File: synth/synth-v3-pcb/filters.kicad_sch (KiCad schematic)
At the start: 44 parts, among them J4 3.5mm Jack, U1 LM324N, U2 LM324N, U3 LM324N, U6 NJM4580D

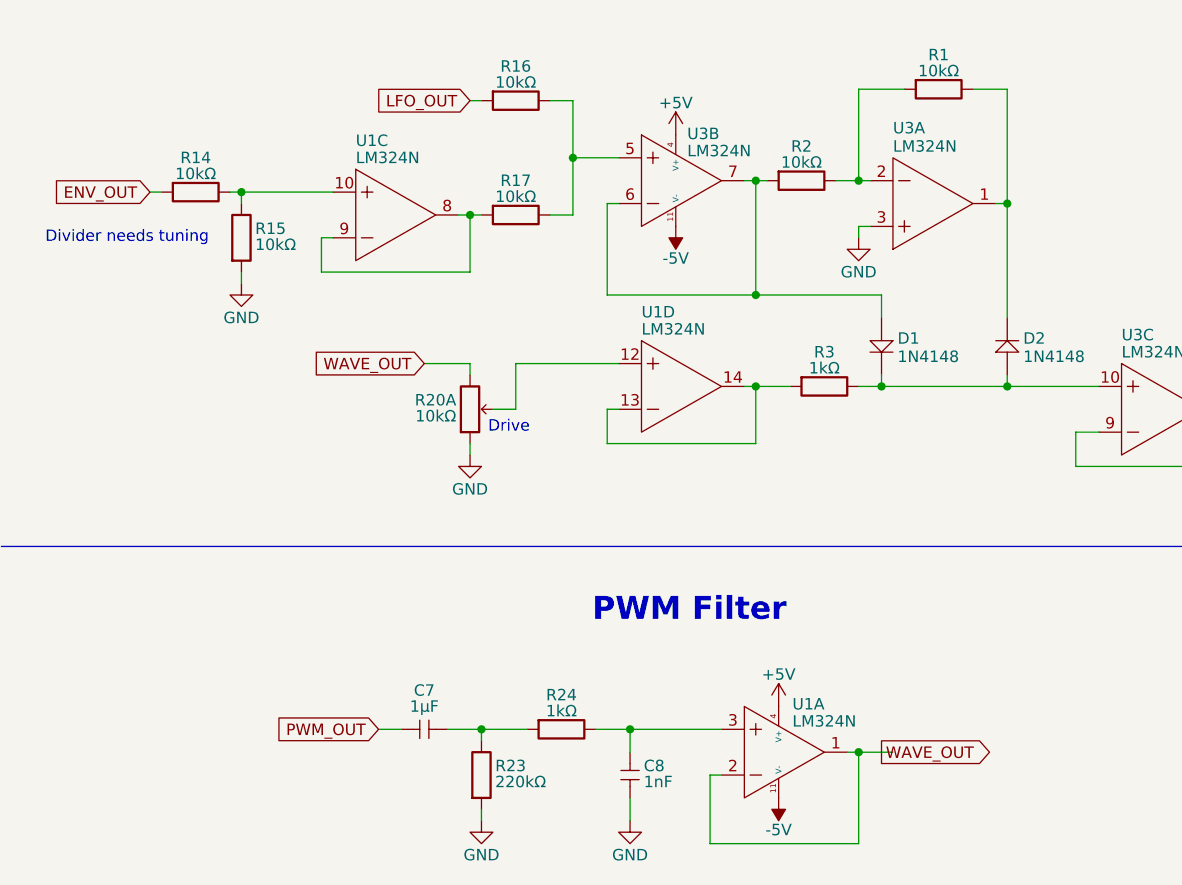
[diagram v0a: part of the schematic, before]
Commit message: Released PCB v3.1 and added knobs
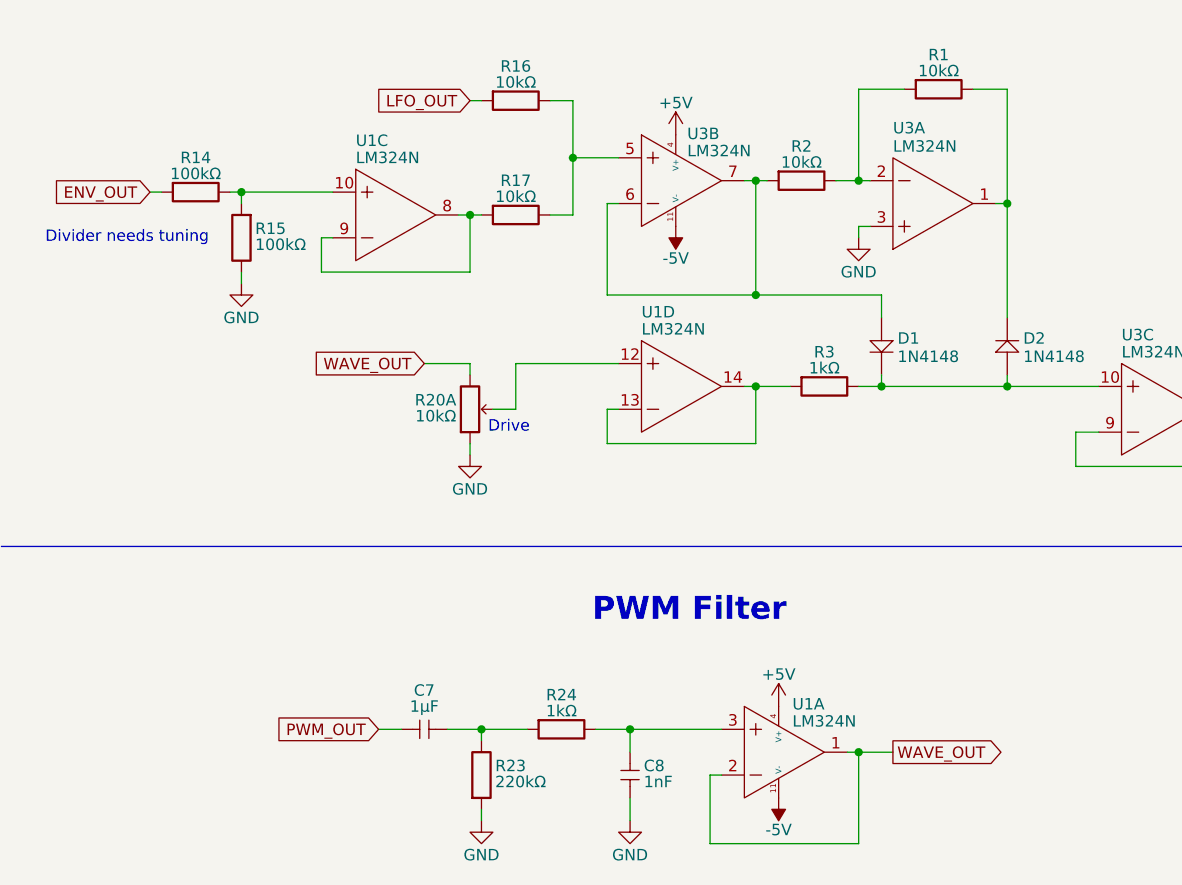
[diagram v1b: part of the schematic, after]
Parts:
- removed R14, R15: 10kΩ, LiveWires:LW_Res, symbol LiveWires:LW_R-10K
- added R14, R15: 100kΩ, LiveWires:LW_Res, symbol LiveWires:LW_R-100K
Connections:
- net ENV_OUT: now also R14.1
- net GND: now also R15.2
- net at U1.10 (IN+): now also R14.2, R15.1
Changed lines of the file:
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@@
 	(global_label "WAVE_OUT"
 		(shape output)
-		(at 114.3 172.72 0)
+		(at 115.57 172.72 0)
 		(fields_autoplaced yes)
 		(effects
@@
 		)
 		(property "Intersheetrefs" "${INTERSHEET_REFS}"
-			(at 126.659 172.72 0)
+			(at 127.929 172.72 0)
 			(effects
 				(font
@@
 	)
 	(symbol
+		(lib_id "LiveWires:LW_R-100K")
+		(at 38.1 110.49 0)
+		(unit 1)
+		(exclude_from_sim no)
+		(in_bom yes)
+		(on_board yes)
+		(dnp no)
+		(property "Reference" "R14"
+			(at 38.1 106.68 0)
+			(effects
+				(font
+					(size 1.27 1.27)
+				)
+			)
+		)
+		(property "Value" "100kΩ"
+			(at 38.1 108.458 0)
+			(effects
+				(font
+					(size 1.27 1.27)
+				)
+			)
+		)
+		(property "Footprint" "LiveWires:LW_Res"
+			(at 38.1 110.49 0)
+			(effects
+				(font
+					(size 1.27 1.27)
+				)
+				(hide yes)
+			)
+		)
+		(property "Datasheet" ""
+			(at 38.1 110.49 0)
+			(effects
+				(font
+					(size 1.27 1.27)
+				)
+				(hide yes)
+			)
+		)
+		(property "Description" "100kΩ Through Hole Resistor (Generic)"
+			(at 38.1 110.49 0)
+			(effects
+				(font
+					(size 1.27 1.27)
+				)
+				(hide yes)
+			)
+		)
+		(property "Cost" "0.03"
+			(at 38.1 110.49 0)
+			(effects
+				(font
+					(size 1.27 1.27)
+				)
+				(hide yes)
+			)
+		)
+		(property "MPN" "MF0W4FF1003"
+			(at 38.1 110.49 0)
+			(effects
+				(font
+					(size 1.27 1.27)
+				)
+				(hide yes)
+			)
+		)
+		(property "Manufacturer" "Royal Ohm"
+			(at 38.1 110.49 0)
+			(effects
+				(font
+					(size 1.27 1.27)
+				)
+				(hide yes)
+			)
+		)
+		(pin "2"
+		)
+		(pin "1"
+		)
+		(instances
+			(project ""
+				(path "/e4b14e5f-7937-4e93-a8ca-bc52b5b8338f/4576f5ad-6b83-487b-bf12-b470c4d9d8e7"
+					(reference "R14")
+					(unit 1)
+				)
+			)
+		)
+	)
+	(symbol
 		(lib_id "LiveWires:PTV112-4420A-A103")
 		(at 49.53 50.8 0)
@@
 	(symbol
 		(lib_id "LiveWires:LW_R-10K")
-		(at 43.18 115.57 90)
-		(unit 1)
-		(exclude_from_sim no)
-		(in_bom yes)
-		(on_board yes)
-		(dnp no)
-		(property "Reference" "R15"
-			(at 44.704 114.554 90)
-			(effects
-				(font
-					(size 1.27 1.27)
-				)
-				(justify right)
-			)
-		)
-		(property "Value" "10kΩ"
-			(at 44.704 116.332 90)
-			(effects
-				(font
-					(size 1.27 1.27)
-				)
-				(justify right)
-			)
-		)
-		(property "Footprint" "LiveWires:LW_Res"
-			(at 43.18 115.57 0)
-			(effects
-				(font
-					(size 1.27 1.27)
-				)
-				(hide yes)
-			)
-		)
-		(property "Datasheet" ""
-			(at 43.18 115.57 0)
-			(effects
-				(font
-					(size 1.27 1.27)
-				)
-				(hide yes)
-			)
-		)
-		(property "Description" "10kΩ Through Hole Resistor (Generic)"
-			(at 43.18 115.57 0)
-			(effects
-				(font
-					(size 1.27 1.27)
-				)
-				(hide yes)
-			)
-		)
-		(property "Cost" "0.03"
-			(at 43.18 115.57 0)
-			(effects
-				(font
-					(size 1.27 1.27)
-				)
-				(hide yes)
-			)
-		)
-		(property "MPN" "MF0W4FF1002"
-			(at 43.18 115.57 0)
-			(effects
-				(font
-					(size 1.27 1.27)
-				)
-				(hide yes)
-			)
-		)
-		(property "Manufacturer" "Royal Ohm"
-			(at 43.18 115.57 0)
-			(effects
-				(font
-					(size 1.27 1.27)
-				)
-				(hide yes)
-			)
-		)
-		(pin "1"
-		)
-		(pin "2"
-		)
-		(instances
-			(project "synth-v1"
-				(path "/e4b14e5f-7937-4e93-a8ca-bc52b5b8338f/4576f5ad-6b83-487b-bf12-b470c4d9d8e7"
-					(reference "R15")
-					(unit 1)
-				)
-			)
-		)
-	)
-	(symbol
-		(lib_id "LiveWires:LW_R-10K")
 		(at 115.57 40.64 0)
 		(unit 1)
@@
 	)
 	(symbol
+		(lib_id "LiveWires:LW_R-100K")
+		(at 43.18 115.57 270)
+		(unit 1)
+		(exclude_from_sim no)
+		(in_bom yes)
+		(on_board yes)
+		(dnp no)
+		(property "Reference" "R15"
+			(at 44.704 114.554 90)
+			(effects
+				(font
+					(size 1.27 1.27)
+				)
+				(justify left)
+			)
+		)
+		(property "Value" "100kΩ"
+			(at 44.704 116.332 90)
+			(effects
+				(font
+					(size 1.27 1.27)
+				)
+				(justify left)
+			)
+		)
+		(property "Footprint" "LiveWires:LW_Res"
+			(at 43.18 115.57 0)
+			(effects
+				(font
+					(size 1.27 1.27)
+				)
+				(hide yes)
+			)
+		)
+		(property "Datasheet" ""
+			(at 43.18 115.57 0)
+			(effects
+				(font
+					(size 1.27 1.27)
+				)
+				(hide yes)
+			)
+		)
+		(property "Description" "100kΩ Through Hole Resistor (Generic)"
+			(at 43.18 115.57 0)
+			(effects
+				(font
+					(size 1.27 1.27)
+				)
+				(hide yes)
+			)
+		)
+		(property "Cost" "0.03"
+			(at 43.18 115.57 0)
+			(effects
+				(font
+					(size 1.27 1.27)
+				)
+				(hide yes)
+			)
+		)
+		(property "MPN" "MF0W4FF1003"
+			(at 43.18 115.57 0)
+			(effects
+				(font
+					(size 1.27 1.27)
+				)
+				(hide yes)
+			)
+		)
+		(property "Manufacturer" "Royal Ohm"
+			(at 43.18 115.57 0)
+			(effects
+				(font
+					(size 1.27 1.27)
+				)
+				(hide yes)
+			)
+		)
+		(pin "2"
+		)
+		(pin "1"
+		)
+		(instances
+			(project ""
+				(path "/e4b14e5f-7937-4e93-a8ca-bc52b5b8338f/4576f5ad-6b83-487b-bf12-b470c4d9d8e7"
+					(reference "R15")
+					(unit 1)
+				)
+			)
+		)
+	)
+	(symbol
 		(lib_id "LiveWires:LW_R-1K")
 		(at 107.95 132.08 0)
@@
 					(unit 1)
 				)
-			)
-		)
-	)
-	(symbol
-		(lib_id "LiveWires:LW_R-10K")
-		(at 38.1 110.49 0)
-		(unit 1)
-		(exclude_from_sim no)
-		(in_bom yes)
-		(on_board yes)
-		(dnp no)
-		(property "Reference" "R14"
-			(at 38.1 106.68 0)
-			(effects
-				(font
-					(size 1.27 1.27)
-				)
-			)
-		)
-		(property "Value" "10kΩ"
-			(at 38.1 108.458 0)
-			(effects
-				(font
-					(size 1.27 1.27)
-				)
-			)
-		)
-		(property "Footprint" "LiveWires:LW_Res"
-			(at 38.1 110.49 0)
-			(effects
-				(font
-					(size 1.27 1.27)
-				)
-				(hide yes)
-			)
-		)
-		(property "Datasheet" ""
-			(at 38.1 110.49 0)
-			(effects
-				(font
-					(size 1.27 1.27)
-				)
-				(hide yes)
-			)
-		)
-		(property "Description" "10kΩ Through Hole Resistor (Generic)"
-			(at 38.1 110.49 0)
-			(effects
-				(font
-					(size 1.27 1.27)
-				)
-				(hide yes)
-			)
-		)
-		(property "Cost" "0.03"
-			(at 38.1 110.49 0)
-			(effects
-				(font
-					(size 1.27 1.27)
-				)
-				(hide yes)
-			)
-		)
-		(property "MPN" "MF0W4FF1002"
-			(at 38.1 110.49 0)
-			(effects
-				(font
-					(size 1.27 1.27)
-				)
-				(hide yes)
-			)
-		)
-		(property "Manufacturer" "Royal Ohm"
-			(at 38.1 110.49 0)
-			(effects
-				(font
-					(size 1.27 1.27)
-				)
-				(hide yes)
-			)
-		)
-		(pin "1"
-		)
-		(pin "2"
-		)
-		(instances
-			(project "synth-v1"
-				(path "/e4b14e5f-7937-4e93-a8ca-bc52b5b8338f/4576f5ad-6b83-487b-bf12-b470c4d9d8e7"
-					(reference "R14")
-					(unit 1)
-				)
